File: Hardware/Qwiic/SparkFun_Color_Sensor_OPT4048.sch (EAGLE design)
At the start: 22 parts, among them J1 QWIIC_RIGHT_ANGLE, J2 QWIIC_RIGHT_ANGLE

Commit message: Removes micro outline, adds mini outline
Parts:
- removed JP3: IO, SparkFun-Connectors:CONN_06NO_SILK_NO_POP
- added C1: 0.1uF, SparkFun-Capacitors:0.1UF-0603-25V-(+80/-20%)
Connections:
- net !CS! renamed INT
- net POCI/SA0 renamed ADDR
- net SDA/PICO renamed SDA
- removed net INT1: JP3.2
- removed net INT2: JP3.1
- removed net OCS: JP3.3
- removed net PICO_AUX: JP3.5
- removed net POCI_AUX: JP3.6
- removed net SCX: JP3.4
- net 3.3V: now also C1.1
- net GND: now also C1.2
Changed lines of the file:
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@@
 <part name="JP1" library="SparkFun-Connectors" deviceset="CONN_06" device="NO_SILK_NO_POP" value="IO"/>
 <part name="LOGO3" library="SparkFun-Aesthetics" deviceset="SFE_LOGO_NAME_FLAME" device=".1_INCH" value="SFE_LOGO_NAME_FLAME.1_INCH"/>
-<part name="JP3" library="SparkFun-Connectors" deviceset="CONN_06" device="NO_SILK_NO_POP" value="IO"/>
 <part name="J1" library="SparkFun-Connectors" deviceset="QWIIC_CONNECTOR" device="JS-1MM" value="QWIIC_RIGHT_ANGLE"/>
 <part name="FD1" library="SparkFun-Aesthetics" deviceset="FIDUCIAL" device="UFIDUCIAL"/>
@@
 <part name="GND7" library="SparkFun-PowerSymbols" deviceset="GND" device=""/>
 <part name="STANDOFF4" library="SparkFun-Hardware" deviceset="STAND-OFF" device="TIGHT"/>
+<part name="C1" library="SparkFun-Capacitors" deviceset="0.1UF" device="-0603-25V-(+80/-20%)" value="0.1uF"/>
+<part name="SUPPLY4" library="SparkFun-PowerSymbols" deviceset="3.3V" device=""/>
+<part name="GND1" library="SparkFun-PowerSymbols" deviceset="GND" device=""/>
 </parts>
 <sheets>
@@
 </instance>
 <instance part="LOGO3" gate="G$1" x="190.5" y="33.02" smashed="yes"/>
-<instance part="JP3" gate="G$1" x="40.64" y="25.4" smashed="yes" rot="MR180">
-<attribute name="VALUE" x="35.56" y="35.56" size="1.778" layer="96" font="vector" rot="MR180"/>
-<attribute name="NAME" x="35.56" y="14.478" size="1.778" layer="95" font="vector" rot="MR180"/>
-</instance>
 <instance part="J1" gate="G$1" x="93.98" y="33.02" smashed="yes">
 <attribute name="VALUE" x="73.66" y="27.686" size="1.778" layer="96" font="vector" align="top-left"/>
@@
 </instance>
 <instance part="STANDOFF4" gate="G$1" x="243.84" y="30.48" smashed="yes"/>
+<instance part="C1" gate="G$1" x="17.78" y="114.3" smashed="yes">
+<attribute name="NAME" x="19.304" y="117.221" size="1.778" layer="95" font="vector"/>
+<attribute name="VALUE" x="19.304" y="112.141" size="1.778" layer="96" font="vector"/>
+</instance>
+<instance part="SUPPLY4" gate="G$1" x="17.78" y="121.92" smashed="yes">
+<attribute name="VALUE" x="17.78" y="124.714" size="1.778" layer="96" font="vector" align="bottom-center"/>
+</instance>
+<instance part="GND1" gate="1" x="17.78" y="106.68" smashed="yes">
+<attribute name="VALUE" x="17.78" y="106.426" size="1.778" layer="96" font="vector" align="top-center"/>
+</instance>
 </instances>
 <busses>
@@
 <pinref part="GND7" gate="1" pin="GND"/>
 </segment>
+<segment>
+<pinref part="C1" gate="G$1" pin="2"/>
+<pinref part="GND1" gate="1" pin="GND"/>
+<wire x1="17.78" y1="111.76" x2="17.78" y2="109.22" width="0.1524" layer="91"/>
+</segment>
 </net>
 <net name="SCL" class="0">
@@
 </segment>
 </net>
-<net name="SDA/PICO" class="0">
+<net name="SDA" class="0">
 <segment>
 <wire x1="45.72" y1="50.8" x2="50.8" y2="50.8" width="0.1524" layer="91"/>
@@
 </segment>
 </net>
-<net name="!CS!" class="0">
+<net name="INT" class="0">
 <segment>
 <wire x1="45.72" y1="55.88" x2="50.8" y2="55.88" width="0.1524" layer="91"/>
 <label x="50.8" y="55.88" size="1.27" layer="95" font="vector" xref="yes"/>
 <pinref part="JP1" gate="G$1" pin="2"/>
-</segment>
-</net>
-<net name="POCI/SA0" class="0">
-<segment>
-<wire x1="45.72" y1="58.42" x2="50.8" y2="58.42" width="0.1524" layer="91"/>
-<label x="50.8" y="58.42" size="1.27" layer="95" font="vector" xref="yes"/>
-<pinref part="JP1" gate="G$1" pin="1"/>
-</segment>
-</net>
-<net name="PICO_AUX" class="0">
-<segment>
-<pinref part="JP3" gate="G$1" pin="5"/>
-<wire x1="45.72" y1="20.32" x2="50.8" y2="20.32" width="0.1524" layer="91"/>
-<label x="50.8" y="20.32" size="1.27" layer="95" font="vector" xref="yes"/>
-</segment>
-</net>
-<net name="SCX" class="0">
-<segment>
-<pinref part="JP3" gate="G$1" pin="4"/>
-<wire x1="45.72" y1="22.86" x2="50.8" y2="22.86" width="0.1524" layer="91"/>
-<label x="50.8" y="22.86" size="1.27" layer="95" font="vector" xref="yes"/>
-</segment>
-</net>
-<net name="INT1" class="0">
-<segment>
-<pinref part="JP3" gate="G$1" pin="2"/>
-<wire x1="45.72" y1="27.94" x2="50.8" y2="27.94" width="0.1524" layer="91"/>
-<label x="50.8" y="27.94" size="1.27" layer="95" font="vector" xref="yes"/>
-</segment>
-</net>
-<net name="INT2" class="0">
-<segment>
-<pinref part="JP3" gate="G$1" pin="1"/>
-<wire x1="45.72" y1="30.48" x2="50.8" y2="30.48" width="0.1524" layer="91"/>
-<label x="50.8" y="30.48" size="1.27" layer="95" font="vector" xref="yes"/>
 </segment>
 </net>
@@
 <wire x1="215.9" y1="165.1" x2="215.9" y2="167.64" width="0.1524" layer="91"/>
 </segment>
-</net>
-<net name="OCS" class="0">
-<segment>
-<pinref part="JP3" gate="G$1" pin="3"/>
-<wire x1="45.72" y1="25.4" x2="50.8" y2="25.4" width="0.1524" layer="91"/>
-<label x="50.8" y="25.4" size="1.27" layer="95" font="vector" xref="yes"/>
+<segment>
+<pinref part="C1" gate="G$1" pin="1"/>
+<pinref part="SUPPLY4" gate="G$1" pin="3.3V"/>
+<wire x1="17.78" y1="119.38" x2="17.78" y2="121.92" width="0.1524" layer="91"/>
 </segment>
 </net>
@@
 </segment>
 </net>
-<net name="POCI_AUX" class="0">
-<segment>
-<pinref part="JP3" gate="G$1" pin="6"/>
-<wire x1="45.72" y1="17.78" x2="50.8" y2="17.78" width="0.1524" layer="91"/>
-<label x="50.8" y="17.78" size="1.27" layer="95" xref="yes"/>
-</segment>
-</net>
+<net name="ADDR" class="0">
+<segment>
+<pinref part="JP1" gate="G$1" pin="1"/>
+<wire x1="50.8" y1="58.42" x2="45.72" y2="58.42" width="0.1524" layer="91"/>
+<label x="50.8" y="58.42" size="1.27" layer="95" font="vector" xref="yes"/>
+</segment>
+</net>

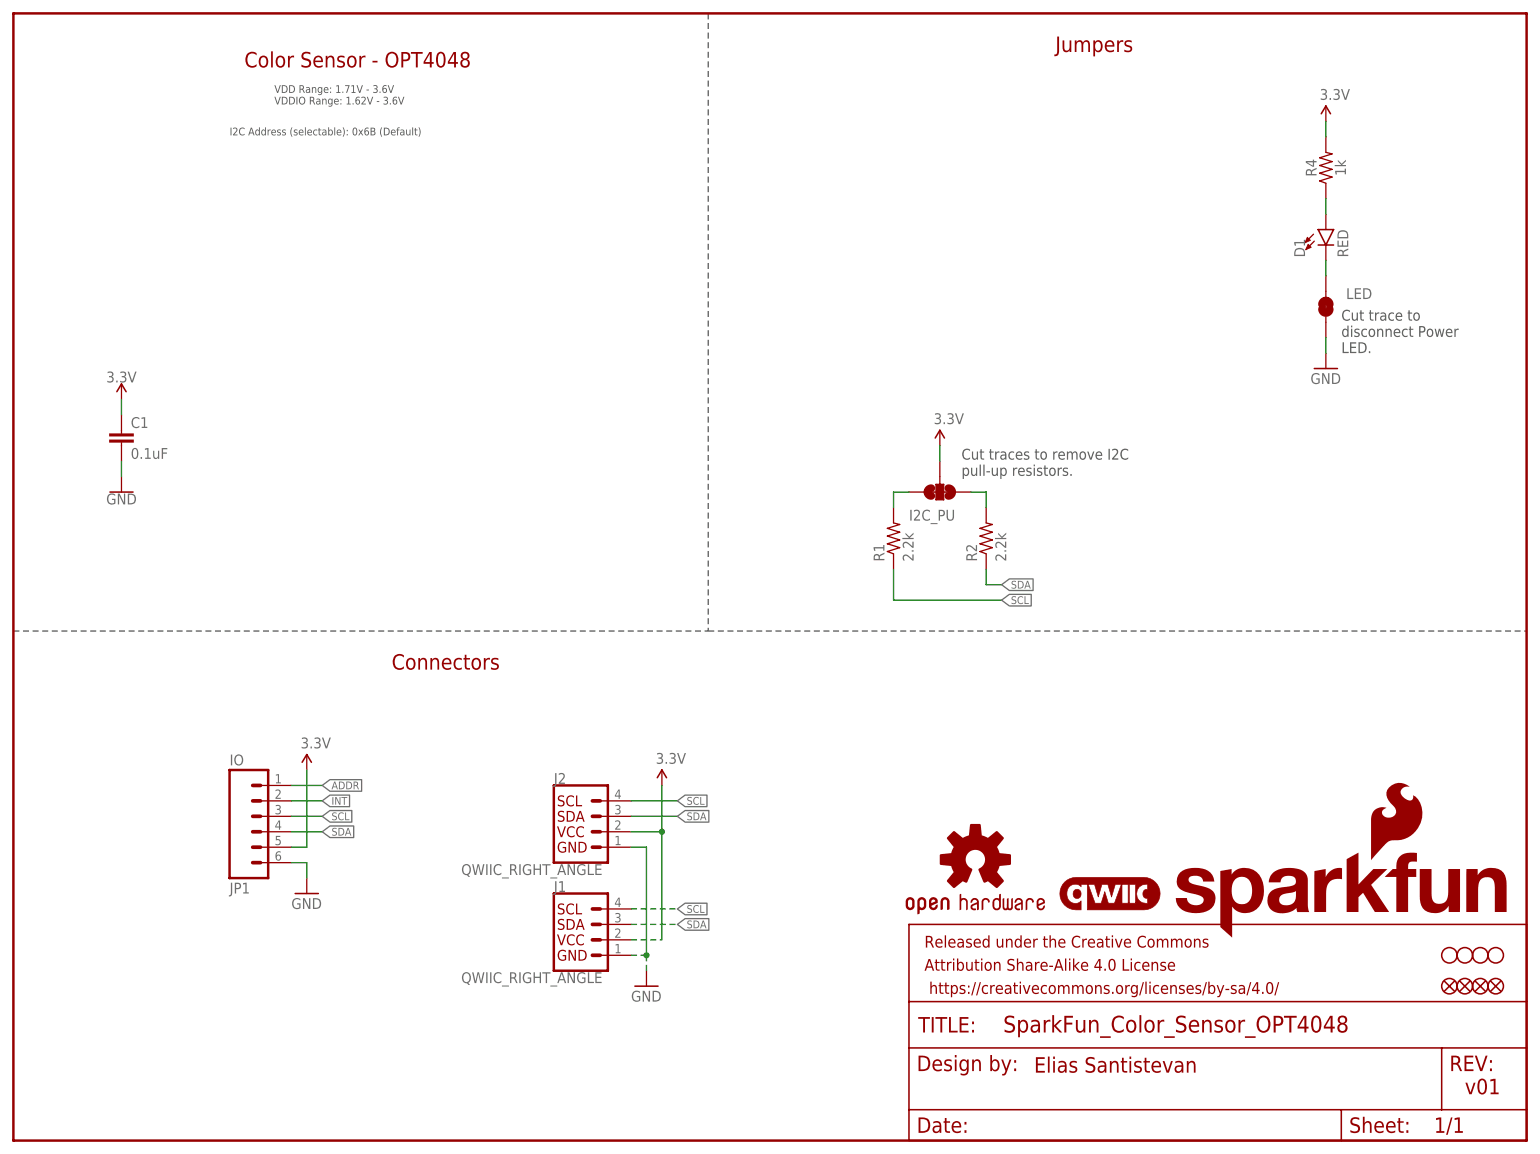
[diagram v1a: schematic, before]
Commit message: Adds OPT4048 device, adds to Qwiic board
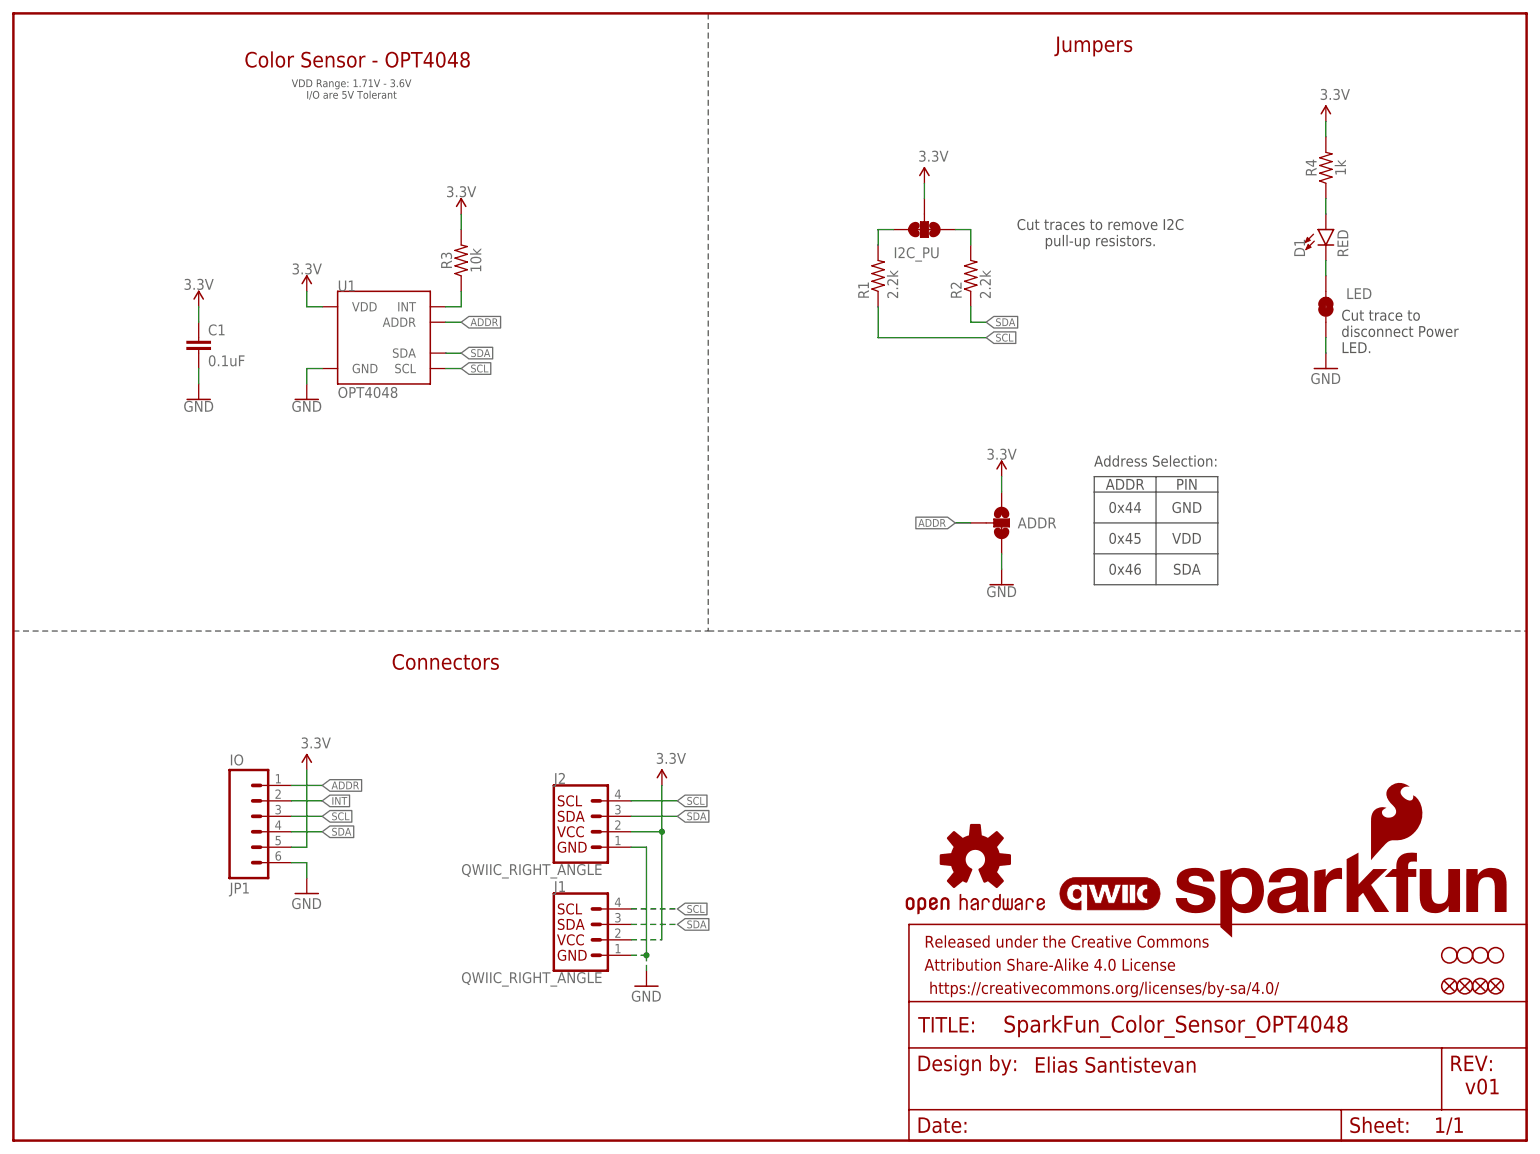
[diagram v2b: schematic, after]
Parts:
- added ADDR: JUMPER-SMT_3_1-NC_TRACE_SILK, SparkFun-Jumpers:JUMPER-SMT_3_1-NC_TRACE_SILK
- added R3: 10k, SparkFun-Resistors:10KOHM-0603-1/10W-1%
- added U1: OPT4048, Color_Sensor:OPT4048
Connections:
- new net N$1: R3.1, U1.INT
- net 3.3V: now also ADDR.1, R3.2, U1.VDD
- net ADDR: now also ADDR.2, U1.ADDR
- net GND: now also ADDR.3, U1.GND
- net SCL: now also U1.SCL
- net SDA: now also U1.SDA
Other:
- note added: "0x44"
- note added: "0x45"
- note added: "0x46"
- note added: "ADDR"
- note added: "Address Selection:"
- note added: "GND"
- note added: "PIN"
- note added: "SDA"
- note added: "VDD"
- note added: "VDD Range: 1.71V - 3.6V I/O are 5V Tolerant"
- note removed: "I2C Address (selectable): 0x6B (Default)"
- note removed: "VDD Range: 1.71V - 3.6V VDDIO Range: 1.62V - 3.6V"
- moved on the sheet: C1, I2C_PU, R1, R2

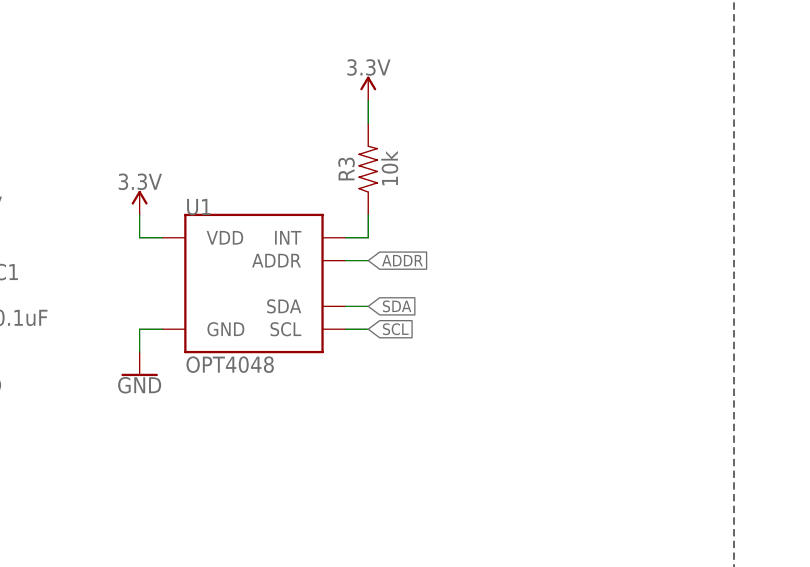
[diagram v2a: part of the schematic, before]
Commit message: Routes the Qwiic board
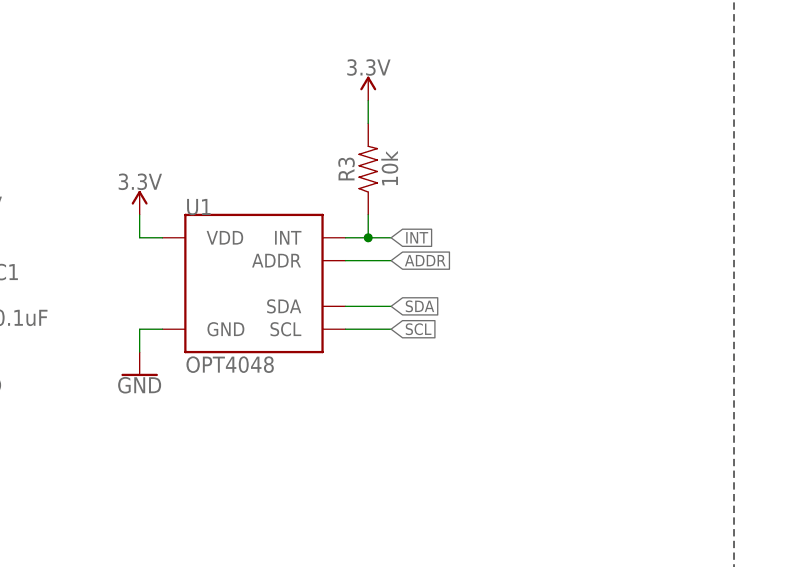
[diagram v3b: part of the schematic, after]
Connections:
- removed net N$1: R3.1, U1.INT
- net INT: now also R3.1, U1.INT
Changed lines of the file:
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@@
 <segment>
 <pinref part="U1" gate="G$1" pin="SCL"/>
-<wire x1="73.66" y1="127" x2="71.12" y2="127" width="0.127" layer="91"/>
-<label x="73.66" y="127" size="1.27" layer="95" font="vector" xref="yes"/>
+<wire x1="76.2" y1="127" x2="71.12" y2="127" width="0.127" layer="91"/>
+<label x="76.2" y="127" size="1.27" layer="95" font="vector" xref="yes"/>
 </segment>
 </net>
@@
 <segment>
 <pinref part="U1" gate="G$1" pin="SDA"/>
-<wire x1="73.66" y1="129.54" x2="71.12" y2="129.54" width="0.127" layer="91"/>
-<label x="73.66" y="129.54" size="1.27" layer="95" font="vector" xref="yes"/>
+<wire x1="76.2" y1="129.54" x2="71.12" y2="129.54" width="0.127" layer="91"/>
+<label x="76.2" y="129.54" size="1.27" layer="95" font="vector" xref="yes"/>
 </segment>
 </net>
@@
 <label x="50.8" y="55.88" size="1.27" layer="95" font="vector" xref="yes"/>
 <pinref part="JP1" gate="J1" pin="2"/>
+</segment>
+<segment>
+<pinref part="U1" gate="G$1" pin="INT"/>
+<wire x1="73.66" y1="137.16" x2="71.12" y2="137.16" width="0.1524" layer="91"/>
+<wire x1="73.66" y1="139.7" x2="73.66" y2="137.16" width="0.1524" layer="91"/>
+<pinref part="R3" gate="G$1" pin="1"/>
+<label x="76.2" y="137.16" size="1.27" layer="95" font="vector" xref="yes"/>
+<wire x1="73.66" y1="137.16" x2="76.2" y2="137.16" width="0.1524" layer="91"/>
+<junction x="73.66" y="137.16"/>
 </segment>
 </net>
@@
 <segment>
 <pinref part="U1" gate="G$1" pin="ADDR"/>
-<wire x1="73.66" y1="134.62" x2="71.12" y2="134.62" width="0.1524" layer="91"/>
-<label x="73.66" y="134.62" size="1.27" layer="95" font="vector" xref="yes"/>
+<wire x1="76.2" y1="134.62" x2="71.12" y2="134.62" width="0.1524" layer="91"/>
+<label x="76.2" y="134.62" size="1.27" layer="95" font="vector" xref="yes"/>
 </segment>
 <segment>
@@
 </segment>
 </net>
-<net name="N$1" class="0">
-<segment>
-<pinref part="U1" gate="G$1" pin="INT"/>
-<wire x1="73.66" y1="137.16" x2="71.12" y2="137.16" width="0.1524" layer="91"/>
-<wire x1="73.66" y1="139.7" x2="73.66" y2="137.16" width="0.1524" layer="91"/>
-<pinref part="R3" gate="G$1" pin="1"/>
-</segment>
-</net>
